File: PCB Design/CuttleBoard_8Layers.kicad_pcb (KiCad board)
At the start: 8 copper layers, 50 x 50 mm, 178 parts, among them IC1 W25Q256JVEIQ TR, J1 DX07WH24JA3R1200, SW1 SW_Push, SW2 SW_Push, U1 LMR33630CQRNX, U14 STM32H743VIHx, U15 TPS62824ADMQ, U16 ICM-20602, U19 USBLC6-2P6, U20 ACS722xLCTR-10AB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

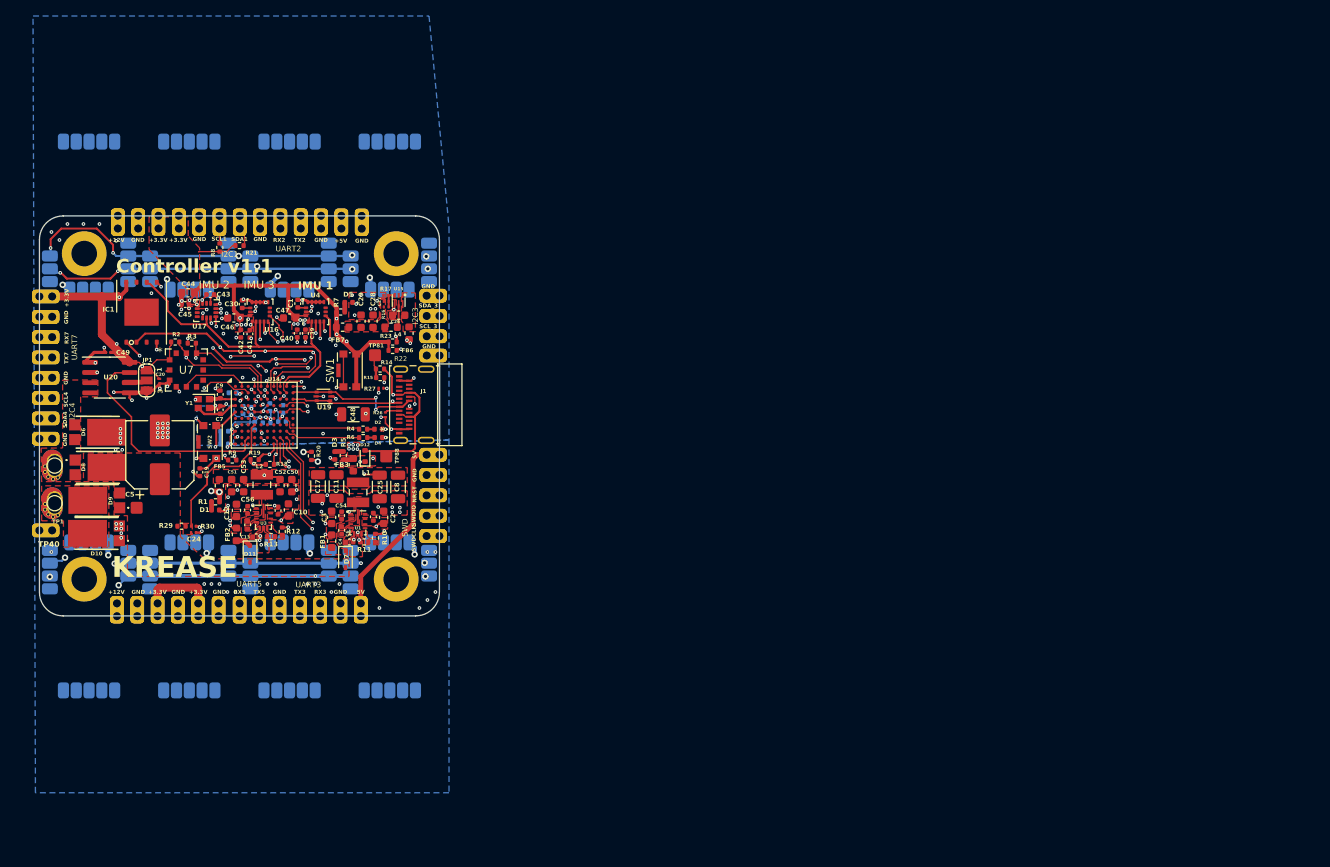
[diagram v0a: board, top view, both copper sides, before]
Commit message: finished BOM for JLCPCB, switched 0201 for 0402, cleaned up silkscreen
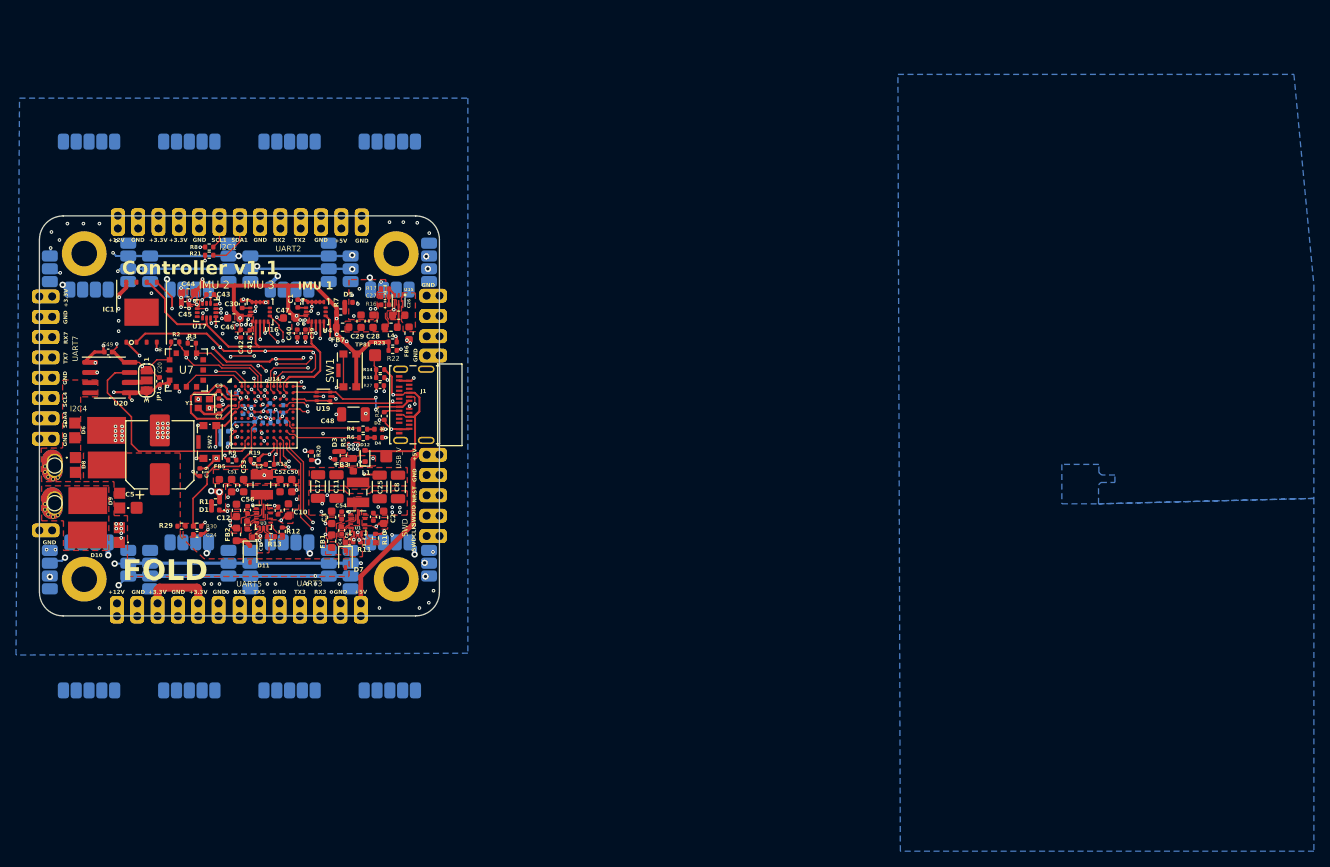
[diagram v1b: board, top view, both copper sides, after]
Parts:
- C20, C24, C27, C49: footprint ultimateFC:C_0201_0603Metric_mod -> Capacitor_SMD:C_0402_1005Metric
- R16, R26, R27: footprint ultimateFC:R_0201_0603Metric_mod -> Capacitor_SMD:C_0402_1005Metric
- R17, R30: footprint ultimateFC:R_0201_0603Metric_mod -> Resistor_SMD:R_0402_1005Metric
- moved R21 3.98 mm to (118.7, 78.9)
- moved R8 1.33 mm to (118.7, 77.9), turned to 0 degrees
- moved R17 0.82 mm to (140.7, 83.1)
- moved C27 0.59 mm to (140.7, 84.1)
- moved C24 0.49 mm to (117.2, 113.8)
- moved R30 0.44 mm to (117.2, 112.8)
- moved R27 0.35 mm to (140.1, 95.2)
- moved D8 0.31 mm to (104.8, 105.1)
- moved R16 0.31 mm to (140.7, 85.1)
- moved D6 0.23 mm to (104.7, 100.8)
- moved R26 0.21 mm to (140.6, 99.0)
- moved D10 0.21 mm to (104.7, 113.9)
- moved C9 0.15 mm to (120.0, 96.3), turned to -90 degrees
- moved C7 0.14 mm to (120.0, 98.2)
- moved R14 0.08 mm to (140.1, 93.2)
- renumbered 5V to +5V
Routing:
- net +3.3V: track 165.1 -> 143.9 mm, vias 34 -> 40
- net GND: track 65.3 -> 81.1 mm, vias 139 -> 146
- net I2C1_SDA: track 24.8 -> 27.9 mm
- net RES_PRESSURE: track 10.4 -> 12.3 mm
- net Net-(U15-FB): track 2.27 -> 3.12 mm
- net SPI3_SCK: track 42.0 -> 42.8 mm
- net I2C1_SCL: track 23.8 -> 24.6 mm
- net CS_FLASH: track 19.2 -> 19.9 mm
- added copper zone on In2.Cu, net +3.3V
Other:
- board text added: "1 2 3 4"
- board text added: "8 7 6 5"
- board text added: "FOLD"
- board text added: "USB_V"
- board text removed: "KREASE"
- board text removed: "University of Manchester 2024"

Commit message: final push
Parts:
- added FISH: LOGO, logo:smug-2, B.Cu at (109.7, 92.6)
- added FISH: LOGO, logo:smug-1, B.Cu at (136.1, 107.5)
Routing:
- net SWDIO: track 25.6 -> 36.6 mm
- net I2C3_SCL: track 22.2 -> 24.4 mm
- net UART5_RX: track 23.5 -> 25.3 mm
- net Net-(C11-Pad1): track 11.6 -> 13.0 mm
- net I2C3_SDA: track 26.1 -> 26.9 mm
- net NRST: track 43.8 -> 43.0 mm
- net I2C1_SDA: track 27.9 -> 28.6 mm
- net UART5_TX: track 24.7 -> 25.3 mm
- net GND: track 81.1 -> 81.4 mm, vias 146 -> 161
- net SPI3_MOSI: track 45.2 -> 45.1 mm, vias 10 -> 8
